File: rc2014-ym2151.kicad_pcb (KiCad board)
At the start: 2 copper layers, 100 x 50 mm, 29 parts, among them CON1 SJ1-3523N, J1 Conn_01x03, P1 RC2014 BUS, U1 74HCT688, U2 YM2151, U3 YM3012, U4 NJM4558, U5 NJM4558, X1 3.579545MHz

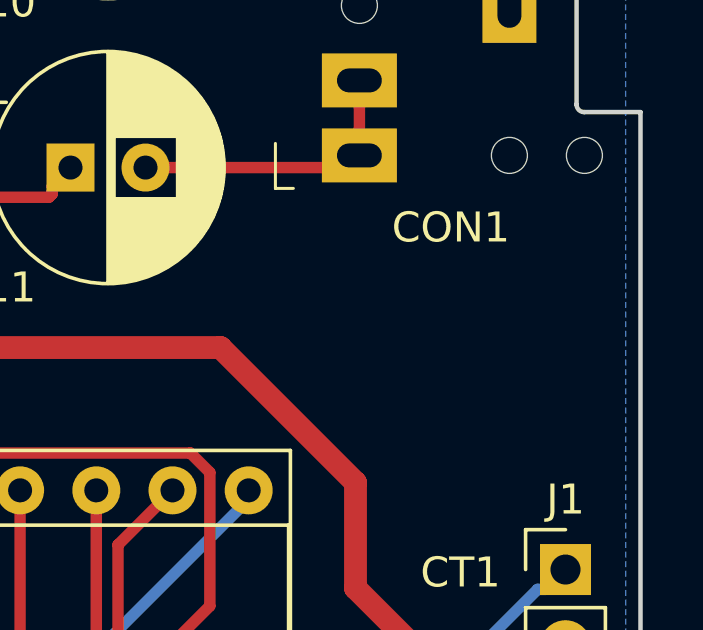
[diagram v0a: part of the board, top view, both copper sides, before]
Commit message: Use git submode for library
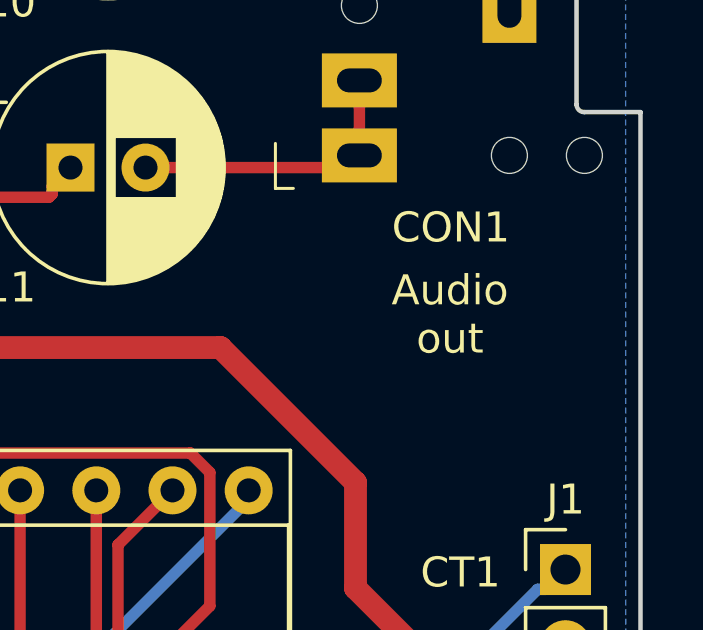
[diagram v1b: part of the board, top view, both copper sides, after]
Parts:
- CON1: footprint rc2014:Headphone_Jack_3.5mm_5_pin -> electrified:Headphone_Jack_3.5mm_5_pin
- G1: footprint rc2014:opm -> electrified:opm
- G2: footprint rc2014:fmsynth -> electrified:fmsynth
- P1: footprint rc2014:PinHeader_1x39_P2.54mm_Vertical -> electrified:PinHeader_1x39_P2.54mm_Vertical
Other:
- board text added: "Audio out"

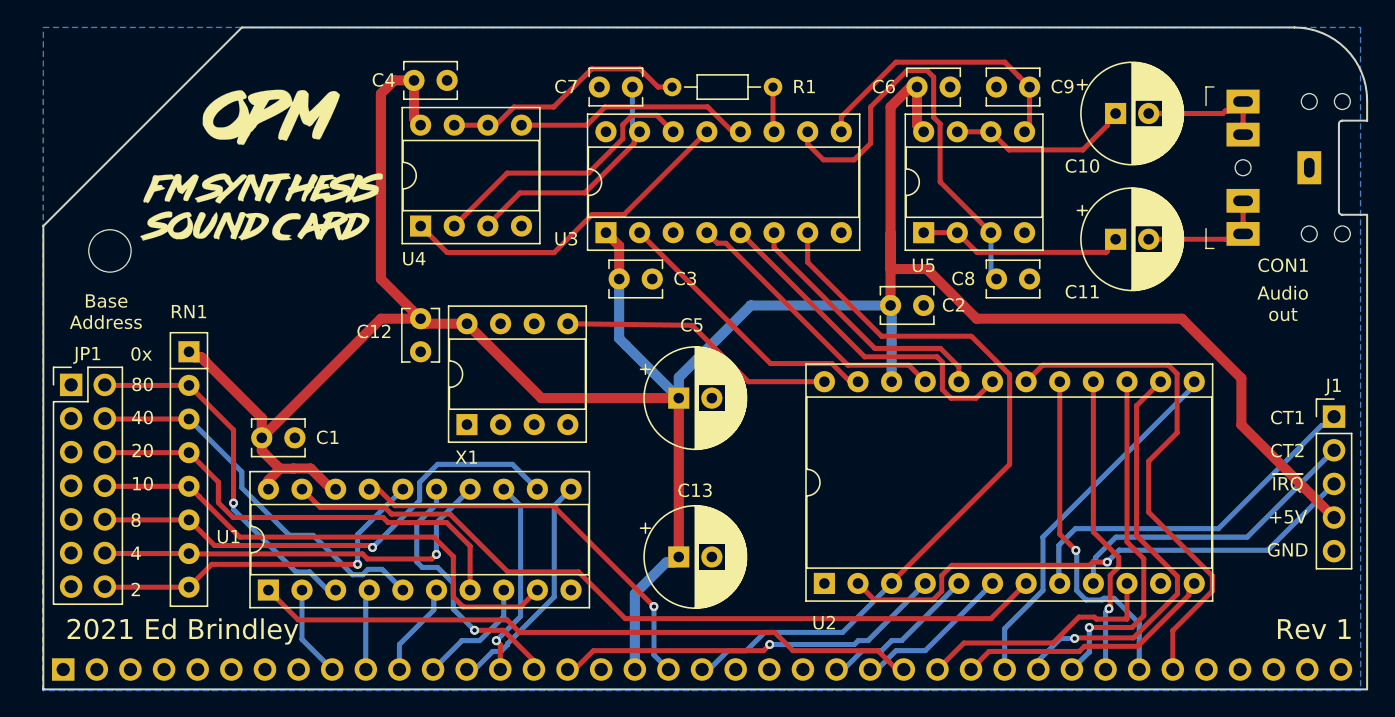
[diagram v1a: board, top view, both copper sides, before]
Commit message: Fix up silkscreen, move opamp location slightly
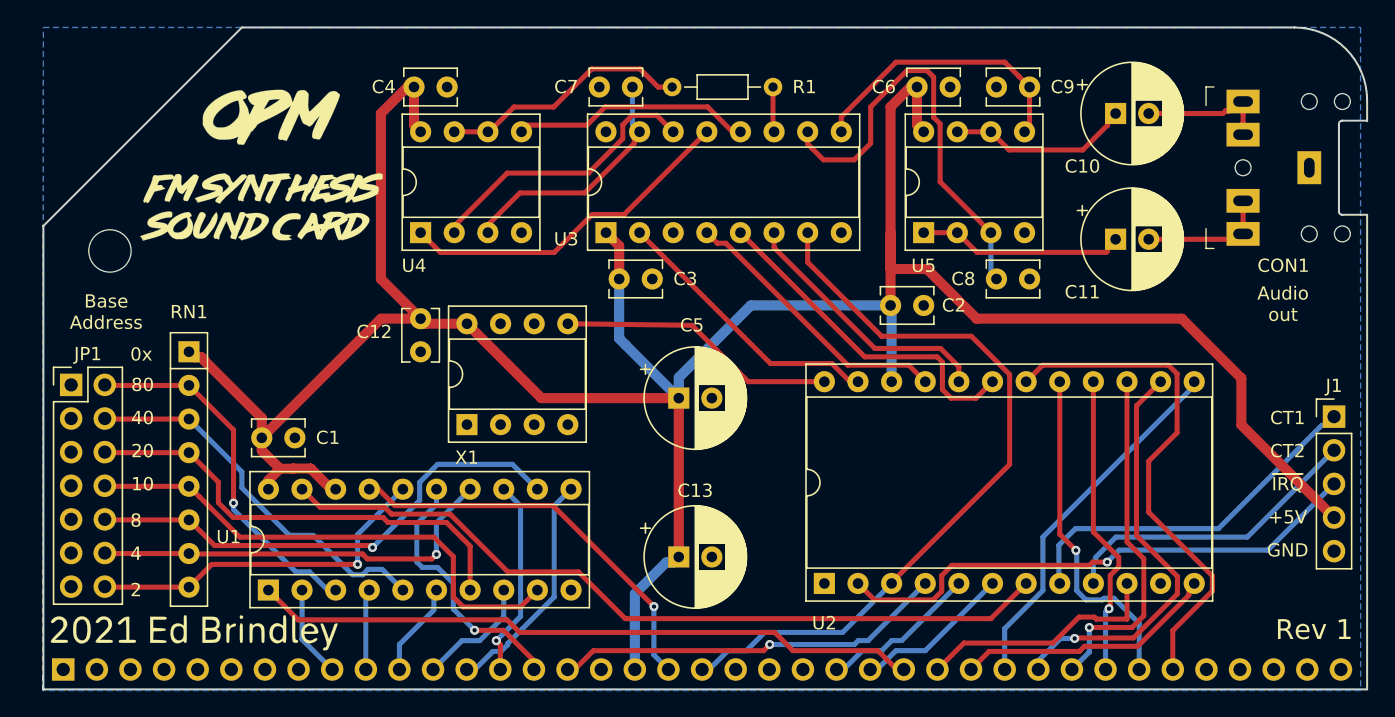
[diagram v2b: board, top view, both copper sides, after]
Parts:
- added G***: LOGO, local:ed_2021, F.Cu at (71.9, 160.2)
- added G***: LOGO, local:algorithm_text, B.Cu at (148.4, 117.5)
- added G***: LOGO, local:envelope_text, B.Cu at (149.0, 138.4)
- added G***: LOGO, local:algorithms, B.Cu at (115.2, 125.9)
- added G***: LOGO, local:envelope, B.Cu at (134.3, 148.8)
- moved G3 3.61 mm to (73.4, 125.7)
- moved C4 0.50 mm to (88.5, 119.0)
- moved U4 0.50 mm to (89.0, 130.0)
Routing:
- net VCC: track 211.1 -> 210.0 mm
- net /BC: track 21.1 -> 21.6 mm
- net /RB: track 18.3 -> 18.8 mm
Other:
- board text removed: "2021 Ed Brindley"

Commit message: Add ability to power opamps separately
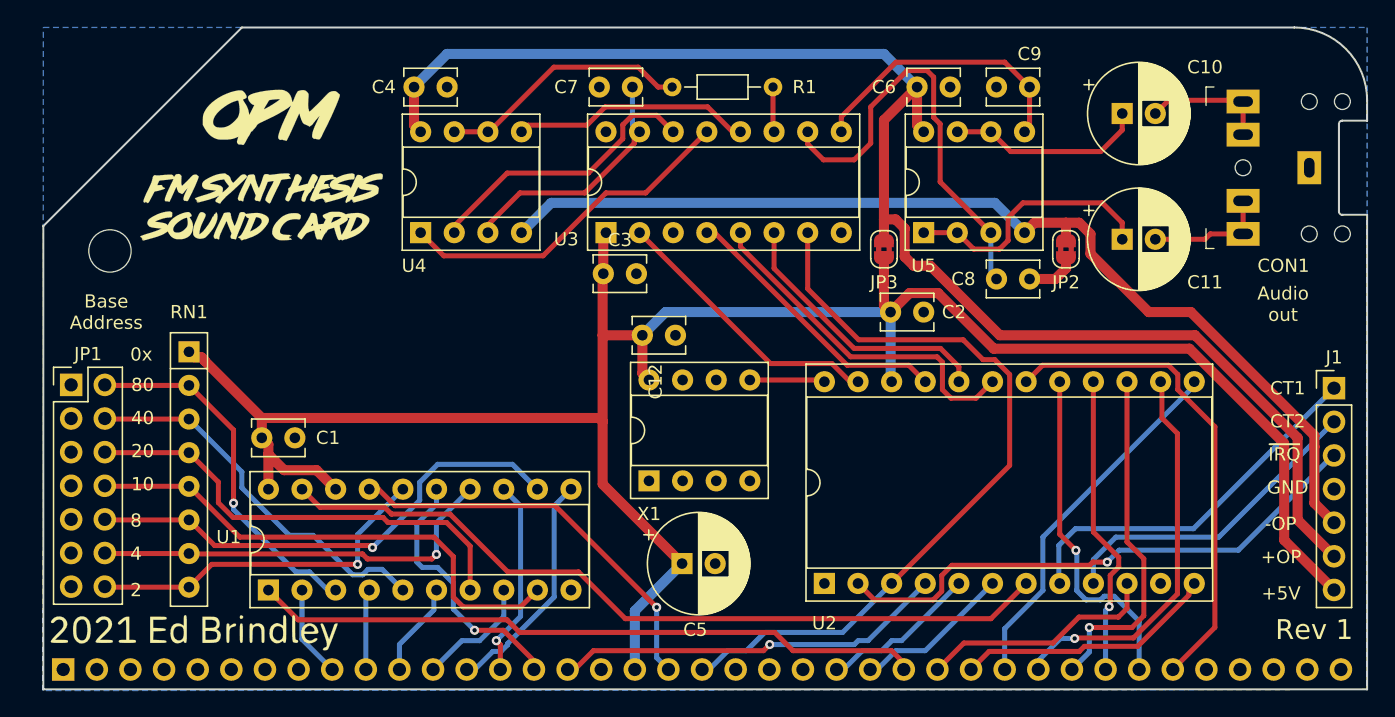
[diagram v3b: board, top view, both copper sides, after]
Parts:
- removed C13: CP_Small, Capacitor_THT:CP_Radial_D7.5mm_P2.50mm
- added JP2: SolderJumper_2_Bridged, Jumper:SolderJumper-2_P1.3mm_Bridged2Bar_RoundedPad1.0x1.5mm, F.Cu at (137.8, 131.2)
- added JP3: SolderJumper_2_Bridged, Jumper:SolderJumper-2_P1.3mm_Bridged2Bar_RoundedPad1.0x1.5mm, F.Cu at (124.0, 131.2)
- C3: value C -> C_Small
- J1: footprint Connector_PinHeader_2.54mm:PinHeader_1x05_P2.54mm_Vertical -> Connector_PinHeader_2.54mm:PinHeader_1x07_P2.54mm_Vertical
- U4, U5: value NJM4558 -> NJM4556
- moved C12 16.8 mm to (105.8, 137.8), turned to 0 degrees
- moved X1 14.4 mm to (106.2, 148.8)
- moved C5 12.5 mm to (108.8, 155.0)
- moved J1 2.15 mm to (158.0, 141.8)
- moved C3 1.26 mm to (102.8, 133.1)
- moved C10 0.50 mm to (142.0, 121.0)
- moved C11 0.50 mm to (142.0, 130.5)
- moved C2 0.50 mm to (124.5, 136.0)
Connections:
- C4 pad 1: VCC -> VDD
- C6 pad 1: VCC -> VDD
- J1 pad 4: VCC -> GND
- J1 pad 5: GND -> VSS
- U4 pad 4: GND -> VSS
- U4 pad 8: VCC -> VDD
- U5 pad 4: GND -> VSS
- U5 pad 8: VCC -> VDD
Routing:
- net VDD: track 0.00 -> 109.3 mm
- net VSS: track 0.00 -> 78.3 mm
- net VCC: track 210.0 -> 165.6 mm
- net /CLK: track 21.1 -> 5.68 mm
- net /R: track 15.7 -> 19.8 mm
- net GND: track 0.00 -> 3.88 mm
- net /D7: track 38.6 -> 37.0 mm
- net /D3: track 31.3 -> 29.8 mm
- net /L: track 13.8 -> 15.0 mm
- net /~RESET: track 57.5 -> 58.7 mm
- net /DAC_SAM1: track 19.9 -> 20.9 mm
- net /CT2: track 23.4 -> 24.3 mm
- net /CT1: track 27.7 -> 28.6 mm
- net /~IRQ: track 40.8 -> 41.7 mm
- net /DAC_SAM2: track 26.0 -> 26.6 mm
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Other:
- board text added: "+OP"
- board text added: "-OP"

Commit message: further updates
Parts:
- removed G2: LOGO, electrified:fmsynth
- added G***: LOGO, local:tone_generator, F.Cu at (76.5, 128.2)
- added G***: LOGO, local:fmsynth, F.Cu at (76.8, 125.0)
- moved G1 1.00 mm to (77.5, 120.0)
